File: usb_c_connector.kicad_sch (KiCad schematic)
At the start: 26 parts, among them J1 USB_C_Receptacle_USB2.0_16P, J2 USB_C_Receptacle_USB2.0_16P, U6 LM66100DCK, U7 LM66100DCK, U8 USBLC6-2SC6, U9 USBLC6-2SC6

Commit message: Use cheaper USB-C connector
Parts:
- J1, J2: footprint Tumbler2:AMPHENOL_10155435-00011LF -> Tumbler2:KINGHELM_KH-TYPE-C-16P; LCSC Part C5409177 -> C709357
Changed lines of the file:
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@@
 			)
 		)
-		(property "Footprint" "Tumbler2:AMPHENOL_10155435-00011LF"
+		(property "Footprint" "Tumbler2:KINGHELM_KH-TYPE-C-16P"
 			(at 193.04 110.49 0)
 			(effects
@@
 			)
 		)
-		(property "LCSC Part" "C5409177"
+		(property "LCSC Part" "C709357"
 			(at 189.23 110.49 0)
 			(effects
@@
 			)
 		)
-		(property "Footprint" "Tumbler2:AMPHENOL_10155435-00011LF"
+		(property "Footprint" "Tumbler2:KINGHELM_KH-TYPE-C-16P"
 			(at 81.28 110.49 0)
 			(effects
@@
 			)
 		)
-		(property "LCSC Part" "C5409177"
+		(property "LCSC Part" "C709357"
 			(at 77.47 110.49 0)
 			(effects

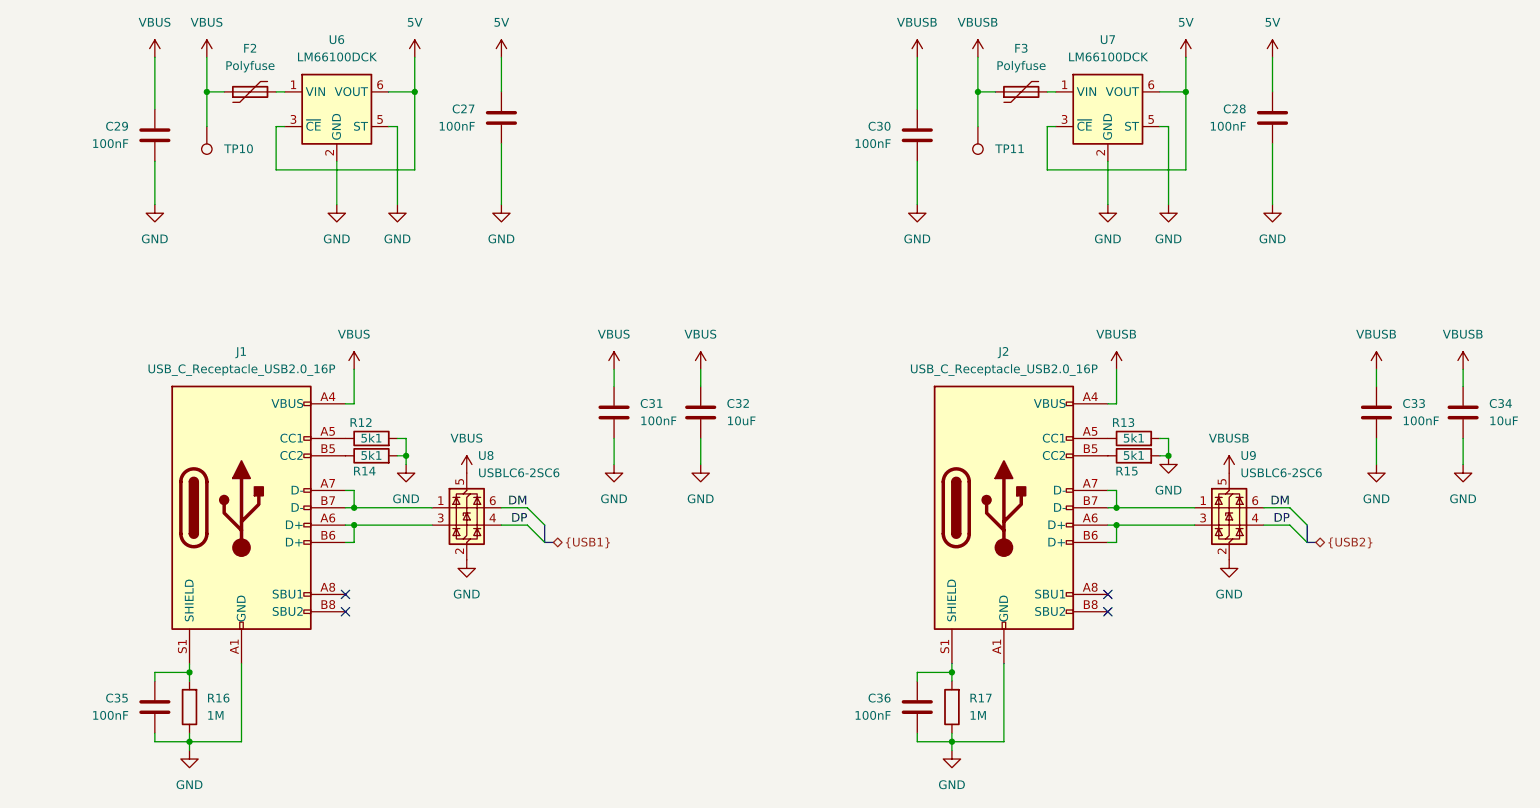
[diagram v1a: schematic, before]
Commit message: Add missing pull-up for CP2102
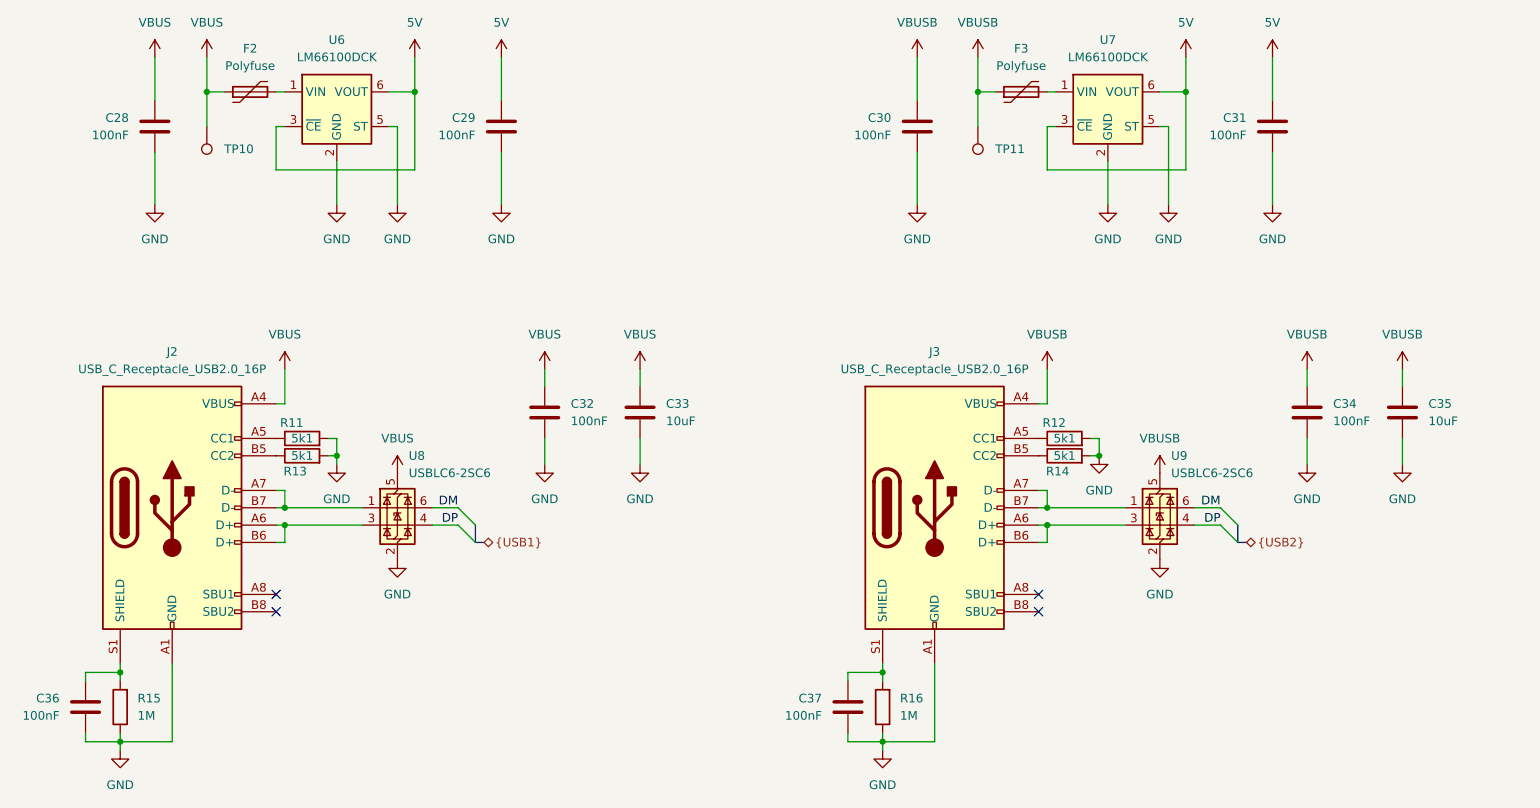
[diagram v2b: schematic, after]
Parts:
- renumbered C29 to C28, C27 to C29, C28 to C31, C31 to C32, C32 to C33, C33 to C34, C34 to C35, C35 to C36, C36 to C37, J1 to J2, J2 to J3, R12 to R11, R13 to R12, R14 to R13, R15 to R14, R16 to R15, R17 to R16
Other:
- moved on the sheet: C28, C29, C30, C31, C32, C33, C34, C35, C36, C37, J2, J3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

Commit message: Remove caps for BTN and GPIO0
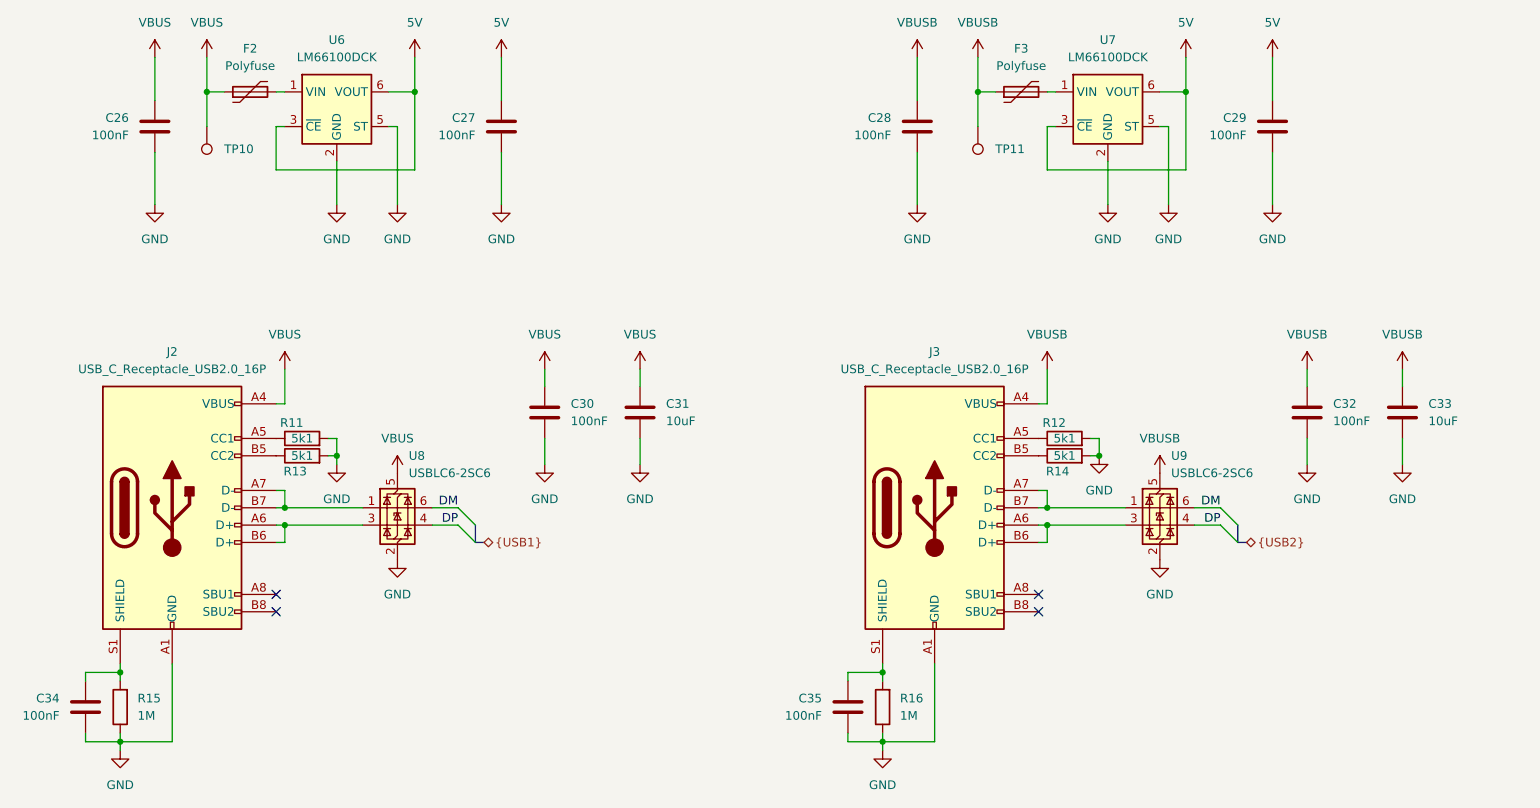
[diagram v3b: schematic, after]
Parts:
- renumbered C28 to C26, C29 to C27, C30 to C28, C31 to C29, C32 to C30, C33 to C31, C34 to C32, C35 to C33, C36 to C34, C37 to C35

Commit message: Add missing bus pull-ups
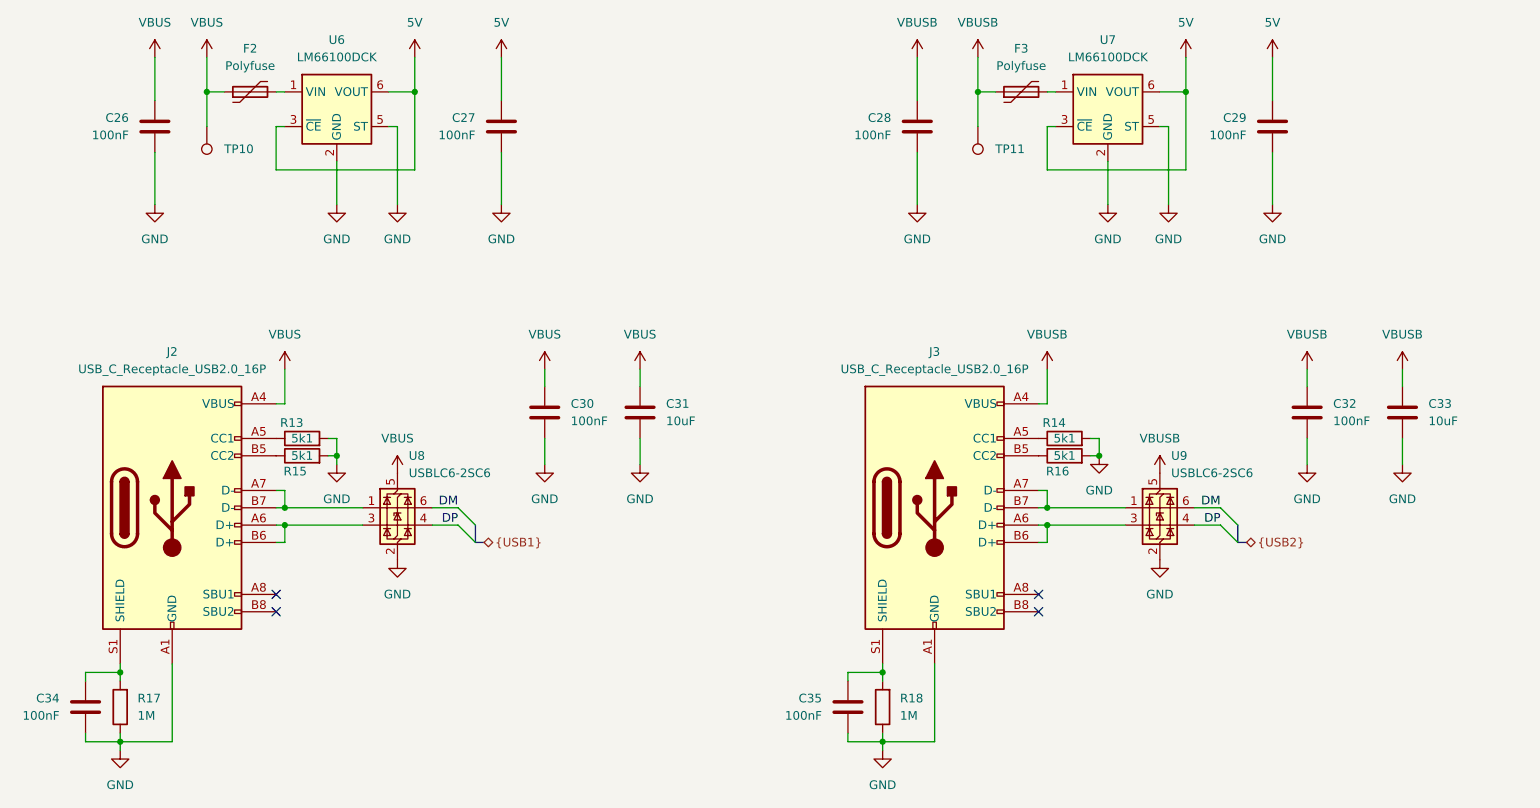
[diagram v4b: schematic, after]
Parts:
- renumbered R11 to R13, R12 to R14, R13 to R15, R14 to R16, R15 to R17, R16 to R18

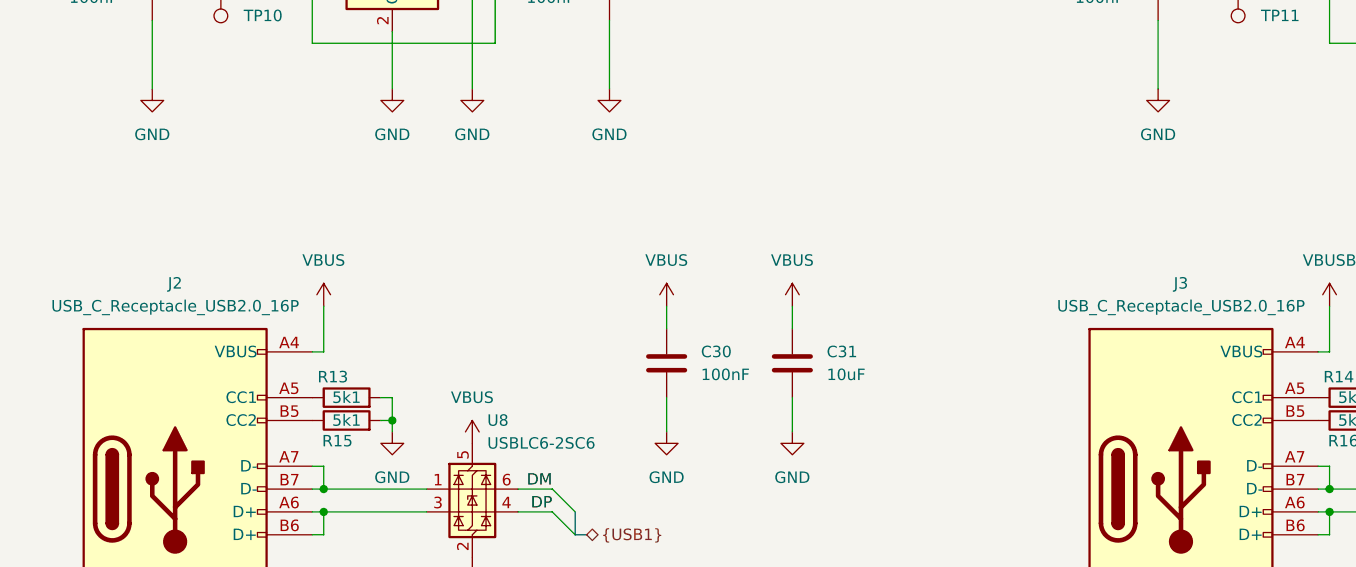
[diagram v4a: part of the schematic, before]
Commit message: Add expansion pin headers
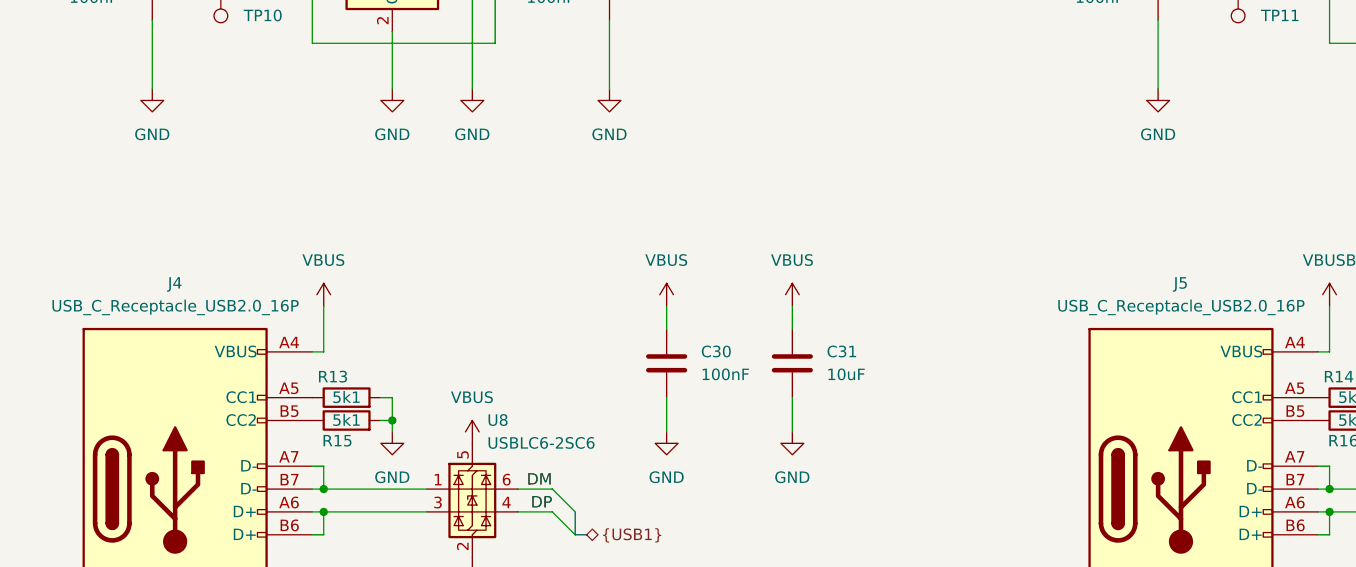
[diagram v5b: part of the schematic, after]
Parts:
- renumbered J2 to J4, J3 to J5

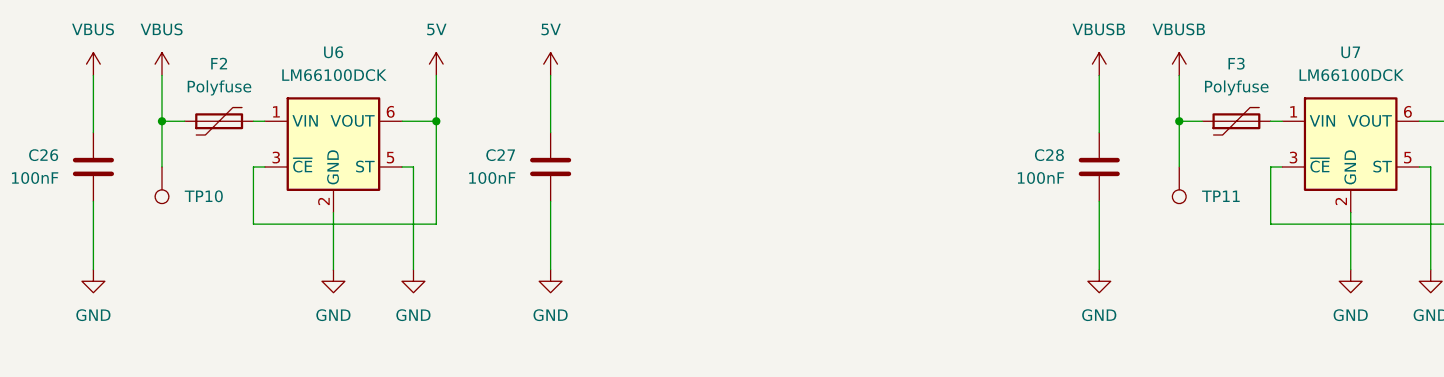
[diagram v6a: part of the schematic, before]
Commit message: Remove polyfuse as not necessary
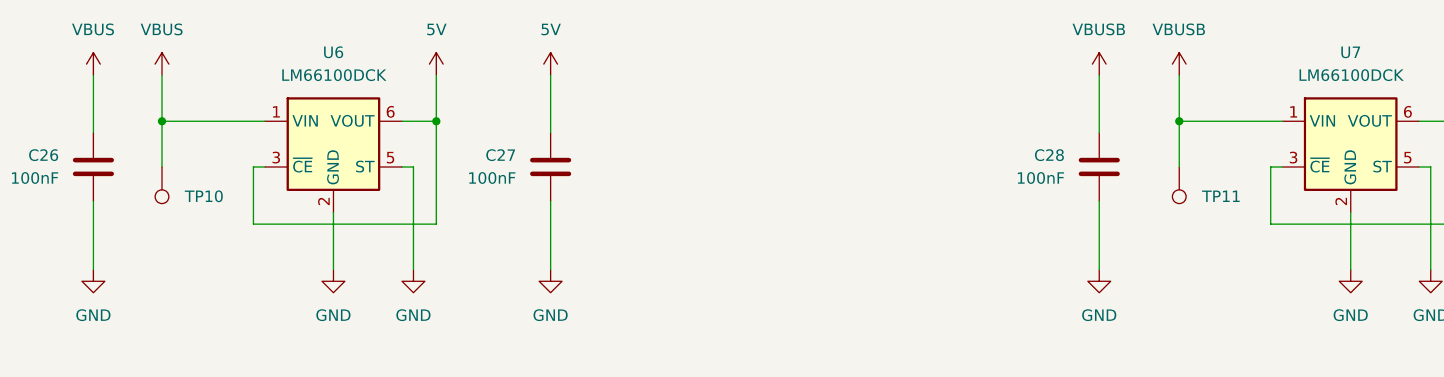
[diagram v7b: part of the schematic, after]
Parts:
- removed F2, F3: Polyfuse, symbol Device:Polyfuse
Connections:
- net VBUS: now also U6.1 (VIN)
- net VBUSB: now also U7.1 (VIN)
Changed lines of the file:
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@@
 	(wire
 		(pts
-			(xy 82.55 49.53) (xy 83.82 49.53)
-		)
-		(stroke
-			(width 0)
-			(type default)
-		)
-	)
-	(wire
-		(pts
 			(xy 213.36 66.04) (xy 213.36 54.61)
 		)
@@
 	(wire
 		(pts
-			(xy 195.58 49.53) (xy 196.85 49.53)
-		)
-		(stroke
-			(width 0)
-			(type default)
-		)
-	)
-	(wire
-		(pts
 			(xy 233.68 104.14) (xy 233.68 100.33)
 		)
@@
 	(wire
 		(pts
-			(xy 187.96 49.53) (xy 185.42 49.53)
+			(xy 185.42 49.53) (xy 196.85 49.53)
 		)
 		(stroke
@@
 	(wire
 		(pts
-			(xy 72.39 49.53) (xy 74.93 49.53)
+			(xy 72.39 49.53) (xy 83.82 49.53)
 		)
 		(stroke
@@
 	)
 	(symbol
-		(lib_id "Device:Polyfuse")
-		(at 78.74 49.53 90)
-		(unit 1)
-		(exclude_from_sim no)
-		(in_bom yes)
-		(on_board yes)
-		(dnp no)
-		(fields_autoplaced yes)
-		(property "Reference" "F2"
-			(at 78.74 43.18 90)
-			(effects
-				(font
-					(size 1.27 1.27)
-				)
-			)
-		)
-		(property "Value" "Polyfuse"
-			(at 78.74 45.72 90)
-			(effects
-				(font
-					(size 1.27 1.27)
-				)
-			)
-		)
-		(property "Footprint" ""
-			(at 83.82 48.26 0)
-			(effects
-				(font
-					(size 1.27 1.27)
-				)
-				(justify left)
-				(hide yes)
-			)
-		)
-		(property "Datasheet" "~"
-			(at 78.74 49.53 0)
-			(effects
-				(font
-					(size 1.27 1.27)
-				)
-				(hide yes)
-			)
-		)
-		(property "Description" "Resettable fuse, polymeric positive temperature coefficient"
-			(at 78.74 49.53 0)
-			(effects
-				(font
-					(size 1.27 1.27)
-				)
-				(hide yes)
-			)
-		)
-		(pin "1"
-		)
-		(pin "2"
-		)
-		(instances
-			(project ""
-				(path "/f3fd8d79-9d35-4c04-811e-2697a2740958/84b20f1f-6e00-4937-92e5-6e005c1bde3e"
-					(reference "F2")
-					(unit 1)
-				)
-			)
-		)
-	)
-	(symbol
 		(lib_id "power:GND")
 		(at 64.77 66.04 0)
@@
 					(unit 1)
 				)
-			)
-		)
-	)
-	(symbol
-		(lib_id "Device:Polyfuse")
-		(at 191.77 49.53 90)
-		(unit 1)
-		(exclude_from_sim no)
-		(in_bom yes)
-		(on_board yes)
-		(dnp no)
-		(fields_autoplaced yes)
-		(property "Reference" "F3"
-			(at 191.77 43.18 90)
-			(effects
-				(font
-					(size 1.27 1.27)
-				)
-			)
-		)
-		(property "Value" "Polyfuse"
-			(at 191.77 45.72 90)
-			(effects
-				(font
-					(size 1.27 1.27)
-				)
-			)
-		)
-		(property "Footprint" ""
-			(at 196.85 48.26 0)
-			(effects
-				(font
-					(size 1.27 1.27)
-				)
-				(justify left)
-				(hide yes)
-			)
-		)
-		(property "Datasheet" "~"
-			(at 191.77 49.53 0)
-			(effects
-				(font
-					(size 1.27 1.27)
-				)
-				(hide yes)
-			)
-		)
-		(property "Description" "Resettable fuse, polymeric positive temperature coefficient"
-			(at 191.77 49.53 0)
-			(effects
-				(font
-					(size 1.27 1.27)
-				)
-				(hide yes)
-			)
-		)
-		(pin "1"
-		)
-		(pin "2"
-		)
-		(instances
-			(project "Tumbler2_Redesign"
-				(path "/f3fd8d79-9d35-4c04-811e-2697a2740958/84b20f1f-6e00-4937-92e5-6e005c1bde3e"
-					(reference "F3")
-					(unit 1)
-				)
